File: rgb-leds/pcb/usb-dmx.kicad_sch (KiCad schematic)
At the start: 24 parts, among them J1 USB_C_Receptacle_USB2.0_16P, J2 USB_A, J3 Conn_01x01_Pin, J4 Conn_01x01_Socket, SW1 PTS526_SM15_SMTR2_LFS, U1 IP4234CZ6, U2 ADP2108AUJ-3.3, U3 ESP32-S3-MINI-1U, U4 ST485E

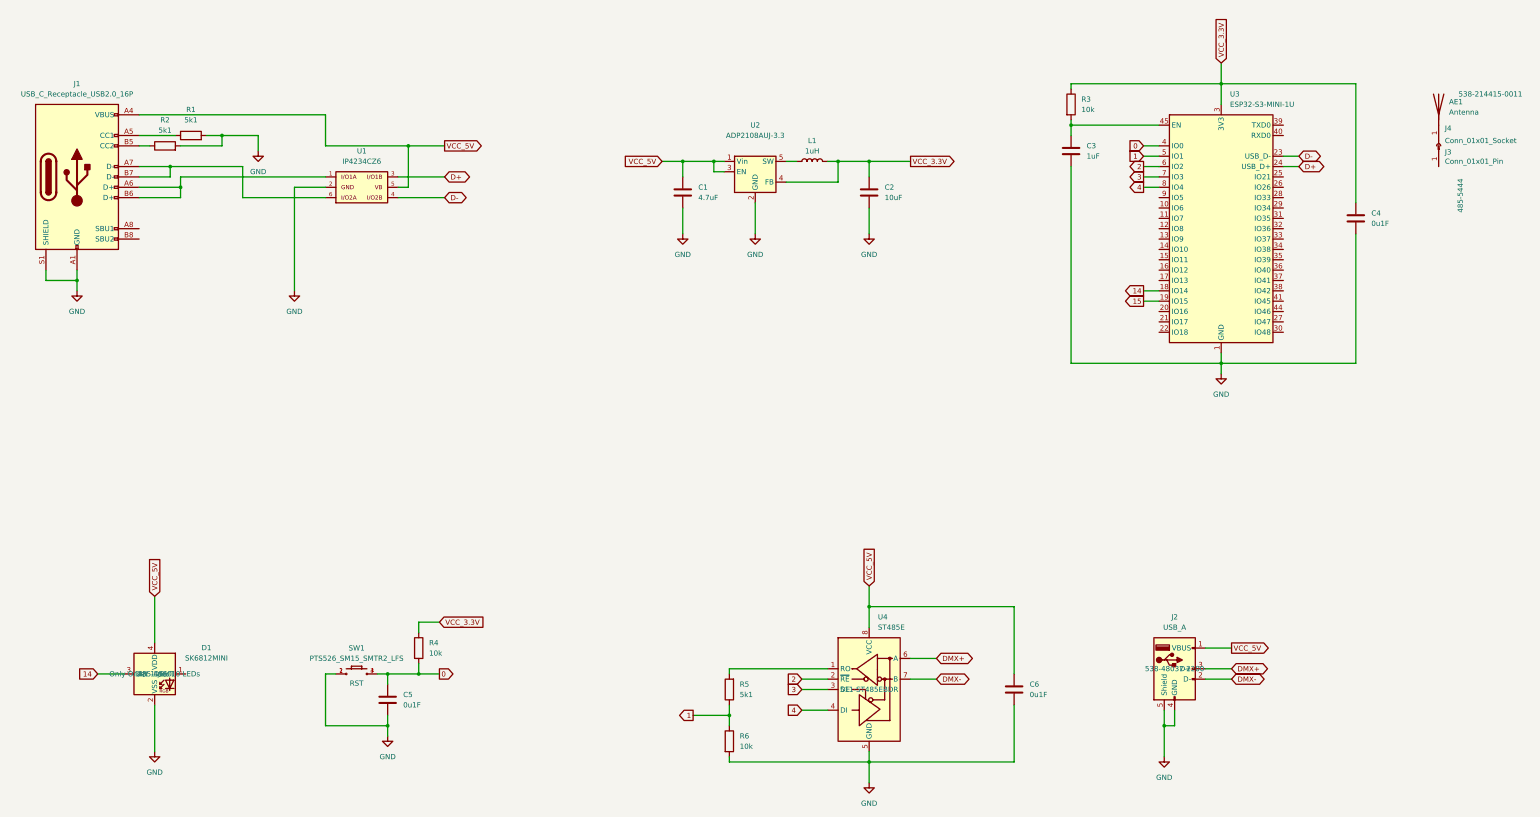
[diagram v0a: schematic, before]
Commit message: fixing pcb, reorganizing firmware library
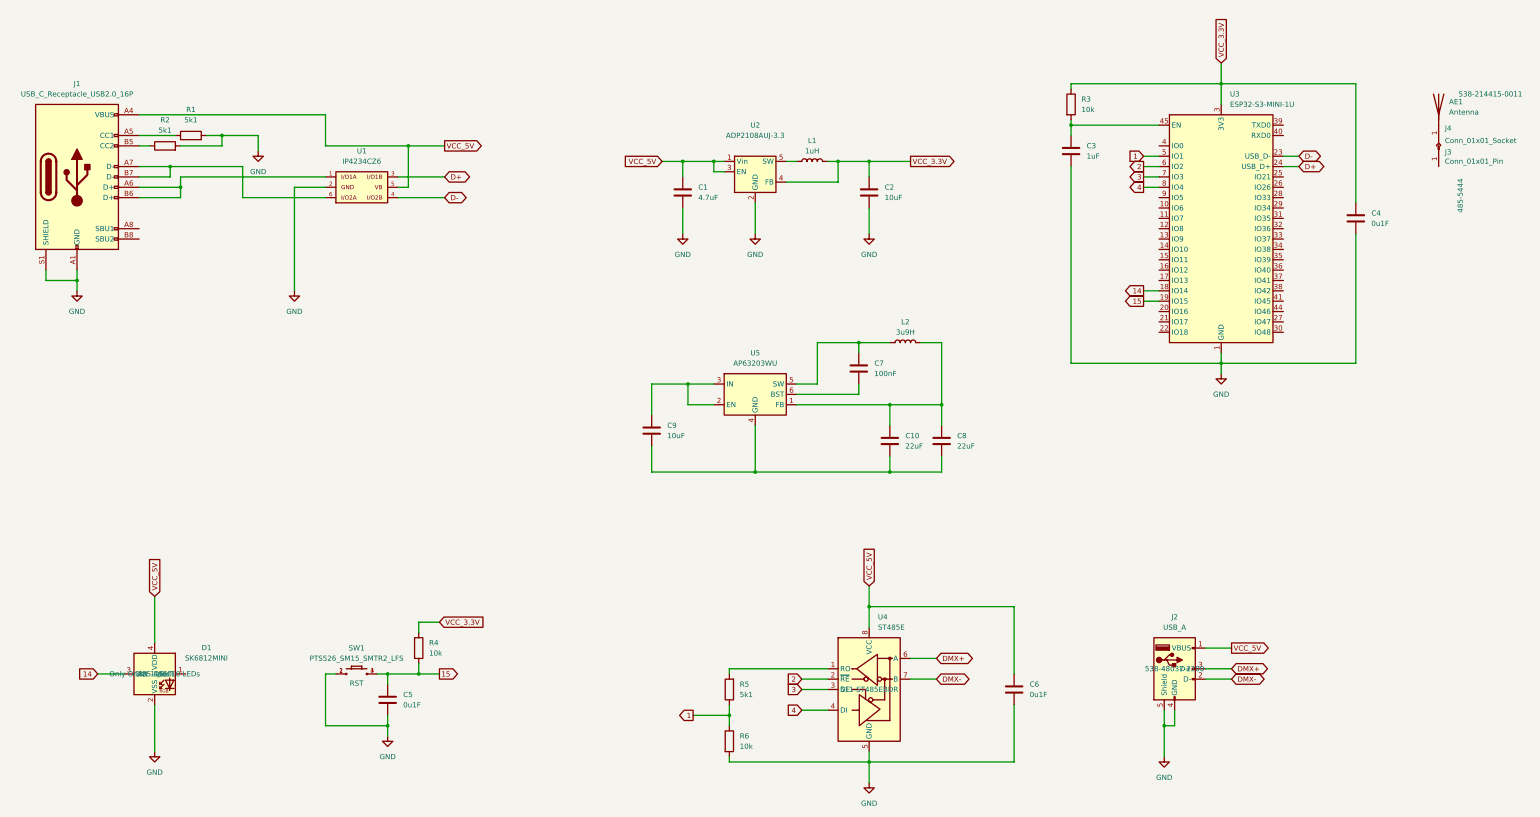
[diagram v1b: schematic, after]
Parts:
- added C10, C8: 22uF, Capacitor_SMD:C_0805_2012Metric, symbol Device:C
- added C7: 100nF, Capacitor_SMD:C_0805_2012Metric, symbol Device:C
- added C9: 10uF, Capacitor_SMD:C_0805_2012Metric, symbol Device:C
- added L2: 3u9H, Inductor_SMD:L_0805_2012Metric, symbol Device:L
- added U5: AP63203WU, Package_TO_SOT_SMD:TSOT-23-6, symbol Regulator_Switching:AP63203WU
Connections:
- net 15: now also C5.1, R4.2, SW1.3, SW1.4
- removed net 0: C5.1, R4.2, SW1.3, SW1.4, U3.4 (IO0)
- new net: C10.1, C8.1, L2.2, U5.1 (FB)
- new net: C10.2, C8.2, C9.2, U5.4 (GND)
- new net: C7.1, L2.1, U5.5 (SW)
- new net: C7.2, U5.6 (BST)
- new net: C9.1, U5.2 (EN), U5.3 (IN)
